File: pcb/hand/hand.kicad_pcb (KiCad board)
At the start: 2 copper layers, 174 x 125.2 mm, 47 parts, among them J1 Conn_01x15, J2 Conn_01x15

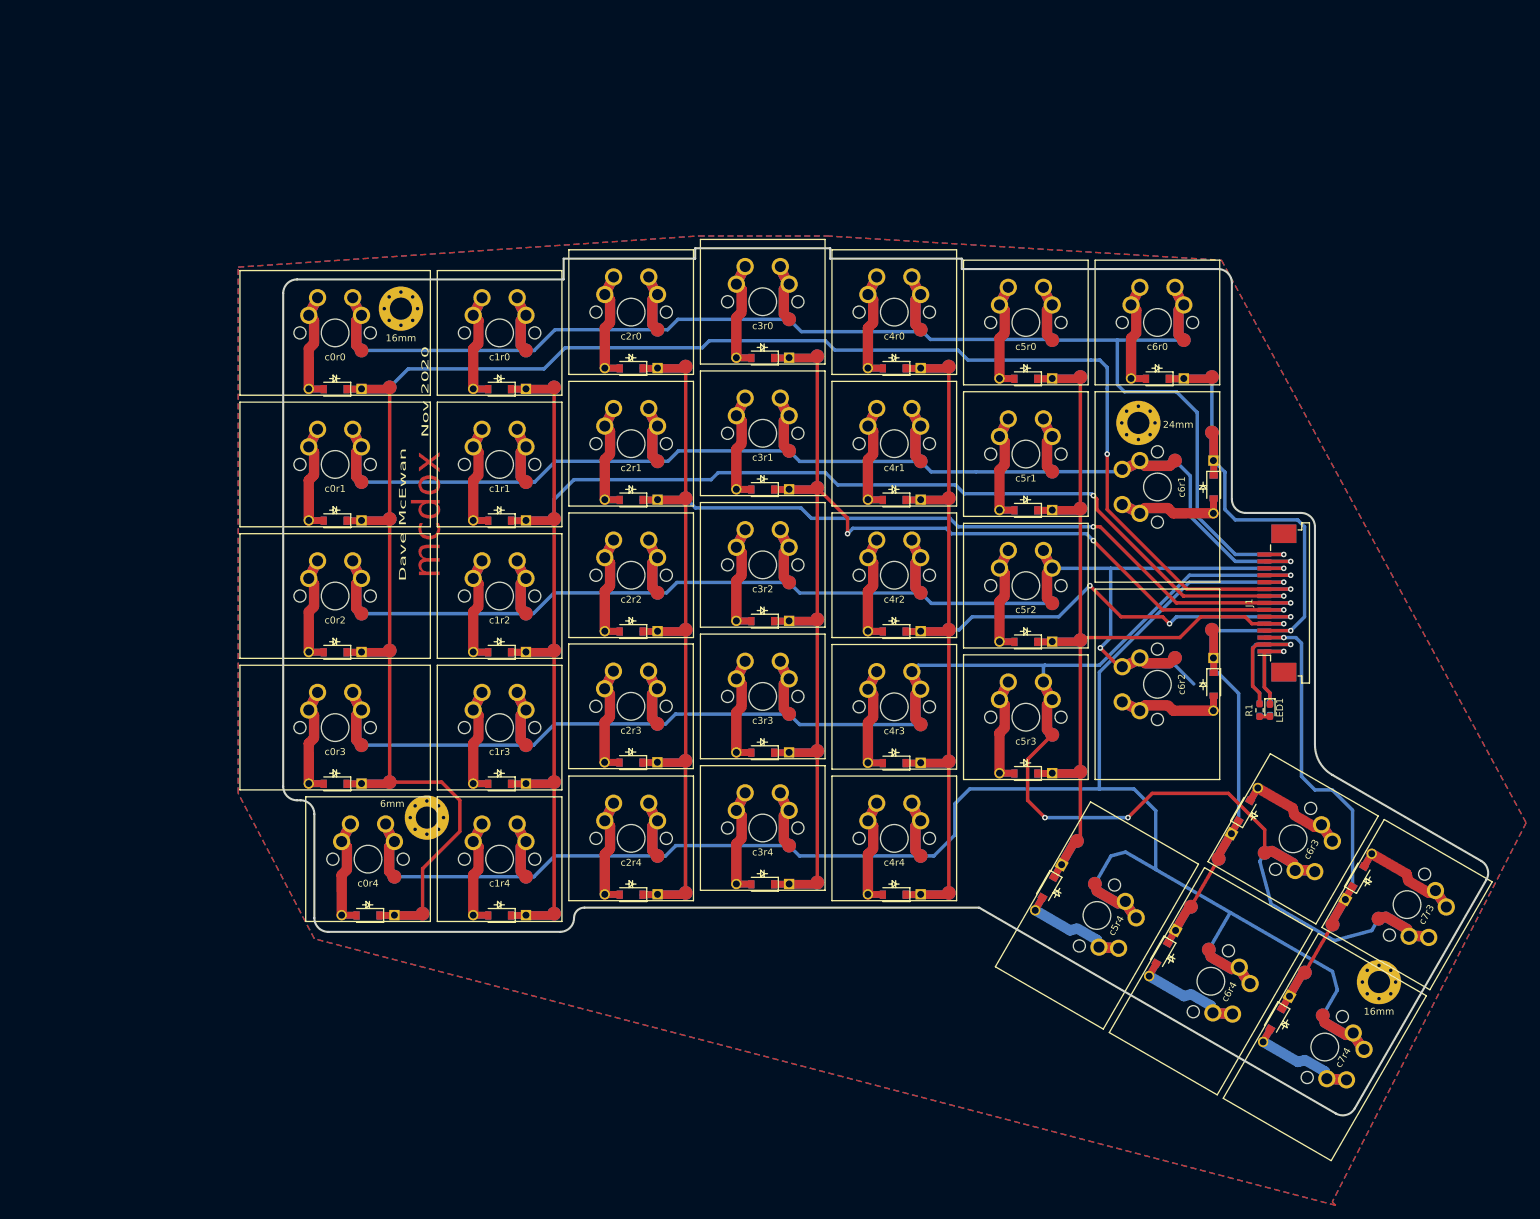
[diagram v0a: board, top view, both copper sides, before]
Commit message: pcb/hand Begin layout and edges.
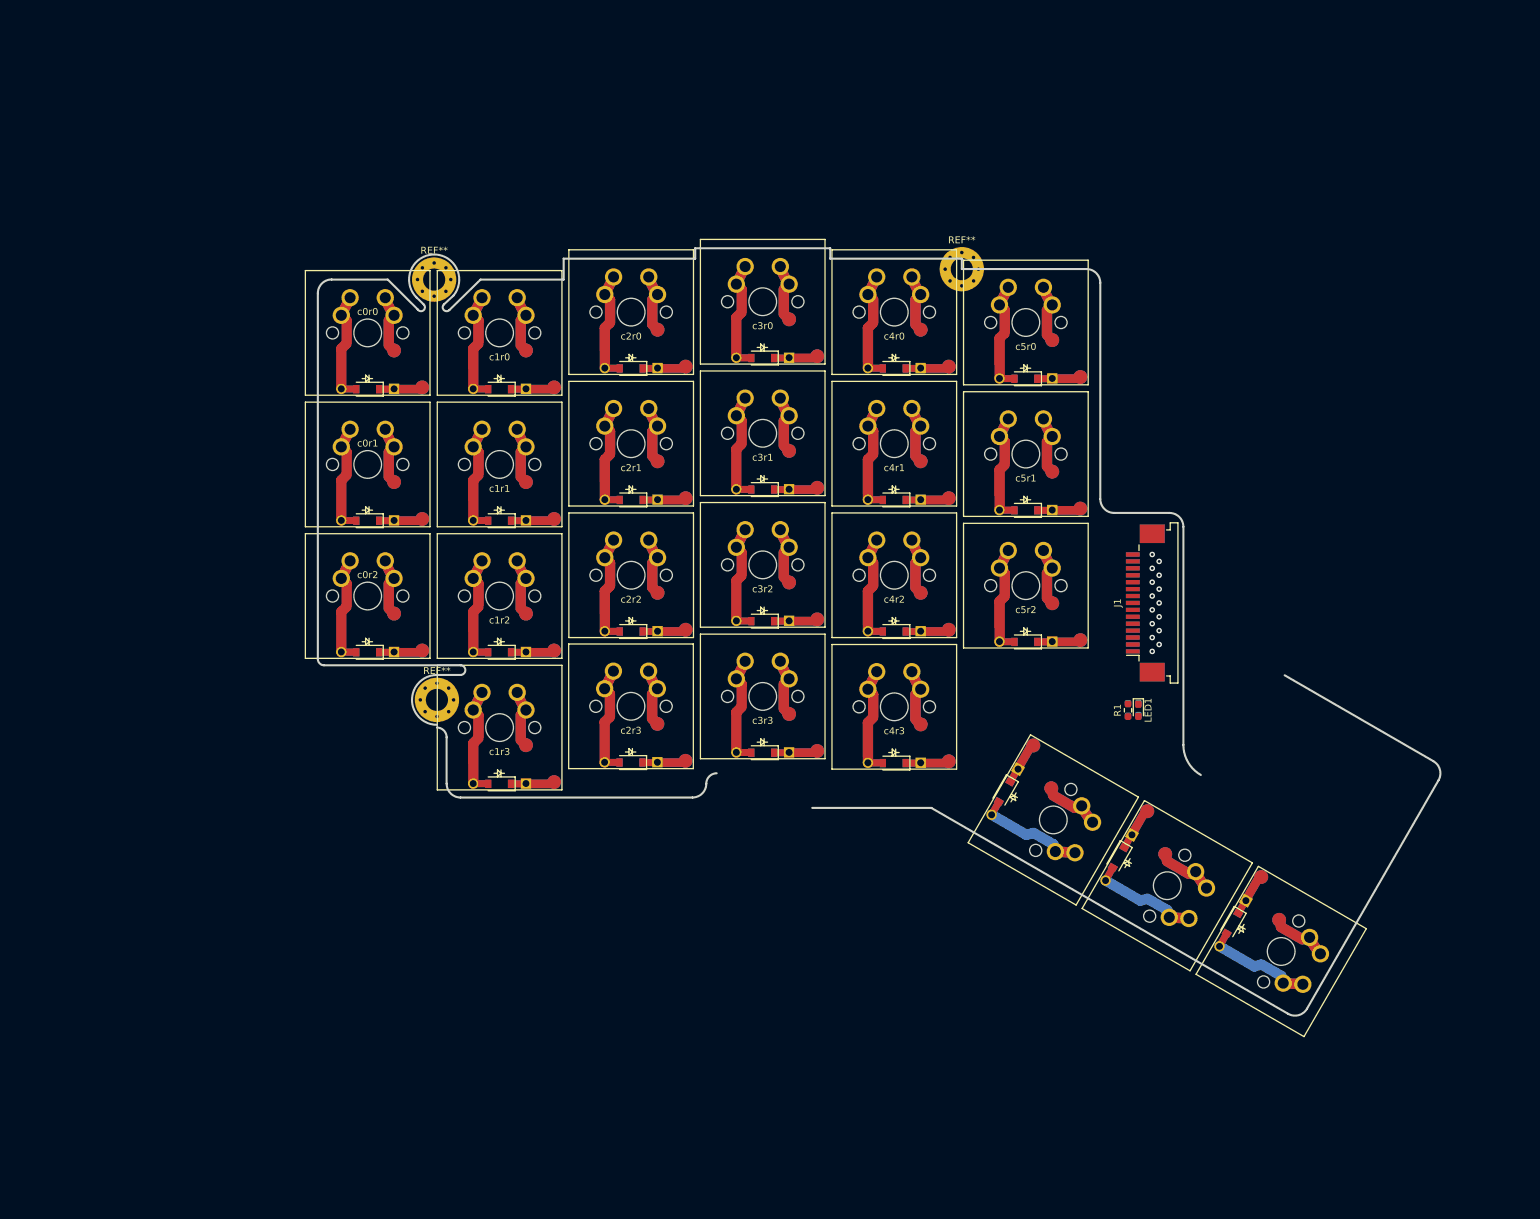
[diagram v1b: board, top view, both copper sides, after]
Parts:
- removed 16mm (x2), 24mm, 6mm: MountingHole_3.2mm_M3_Pad_Via, hand:MountingHole_3.2mm_M3_Pad_Via
- removed c0r3, c5r4, c6r4, c7r4: switchDiode, hand:reversibleMX_15u
- removed c0r4, c1r4, c2r4, c3r4, c4r4, c5r3, c6r0, c7r3: switchDiode, hand:reversibleMX_10u
- added REF**: MountingHole_3.2mm_M3_Pad_Via, hand:MountingHole_3.2mm_M3_Pad_Via, F.Cu at (58.7, 92.0)
- added REF**: MountingHole_3.2mm_M3_Pad_Via, hand:MountingHole_3.2mm_M3_Pad_Via, F.Cu at (134.5, 29.8)
- added REF**: MountingHole_3.2mm_M3_Pad_Via, hand:MountingHole_3.2mm_M3_Pad_Via, F.Cu at (58.3, 31.3)
- R1, R2: value 100 -> 220
- c0r0, c0r1, c0r2: footprint hand:reversibleMX_15u -> hand:reversibleMX_10u
- c6r1, c6r2: footprint hand:reversibleMX_15u -> hand:reversibleMX_10u; moved to B.Cu
- c6r3: moved to B.Cu
- moved c6r1 69.4 mm to (180.6, 128.3), turned to 60 degrees
- moved c6r3 34.7 mm to (147.7, 109.3), turned to 60 degrees
- moved c6r2 29.1 mm to (164.2, 118.8), turned to 60 degrees
- moved J1 19.0 mm to (161.0, 78.0)
- moved J2 19.0 mm to (161.0, 78.0)
- moved LED1 19.0 mm to (160.0, 93.5)
- moved LED2 19.0 mm to (160.0, 93.4)
- moved R1 19.0 mm to (158.5, 93.5)
- moved R2 19.0 mm to (158.5, 93.4)
- moved c0r0 4.70 mm to (48.7, 39.0)
- moved c0r1 4.70 mm to (48.7, 58.0)
- moved c0r2 4.70 mm to (48.7, 77.0)
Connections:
- J1 pad 11: row4 -> Net-(J1-Pad11)
- J1 pad 3: col7 -> Net-(J1-Pad3)
- J2 pad 13: col7 -> Net-(J2-Pad13)
- J2 pad 5: row4 -> Net-(J2-Pad5)
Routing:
- net col0: track 313.4 -> 0.00 mm, vias 2 -> 1
- net row4: track 271.5 -> 0.00 mm
- net row3: track 265.5 -> 0.00 mm, vias 3 -> 1
- net col1: track 261.9 -> 0.00 mm, vias 2 -> 1
- net col2: track 238.5 -> 0.00 mm, vias 2 -> 1
- net col3: track 220.5 -> 0.00 mm, vias 3 -> 1
- net row0: track 206.9 -> 0.00 mm
- net col4: track 199.6 -> 0.00 mm, vias 3 -> 1
- net row2: track 191.9 -> 0.00 mm, vias 2 -> 1
- net row1: track 174.9 -> 0.00 mm
- net col5: track 164.6 -> 0.00 mm
- net col6: track 152.3 -> 0.00 mm
- net col7: track 80.6 -> 0.00 mm
- net +3V3: track 28.3 -> 0.00 mm
- net GND: track 21.4 -> 0.00 mm
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- removed copper zone on B.Cu, net (none)
- removed copper zone on F.Cu, net (none)
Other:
- board size 174 x 125.2 mm -> 162.1 x 110.8 mm
- board text removed: "Dave McEwan"
- board text removed: "Nov 2020"
- board text removed: "c0r5"
- board text removed: "c0r6"
- board text removed: "c1r5"
- board text removed: "c2r5"
- board text removed: "c3r5"
- board text removed: "c4r5"
- board text removed: "c5r5"
- board text removed: "c5r6"
- board text removed: "c6r5"
- board text removed: "c6r6"
- board text removed: "c6r7"
- board text removed: "c6r8"
- board text removed: "c6r9"
- board text removed: "c7r5"
- board text removed: "c7r6"

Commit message: pcb/hand Layout finger cluster.
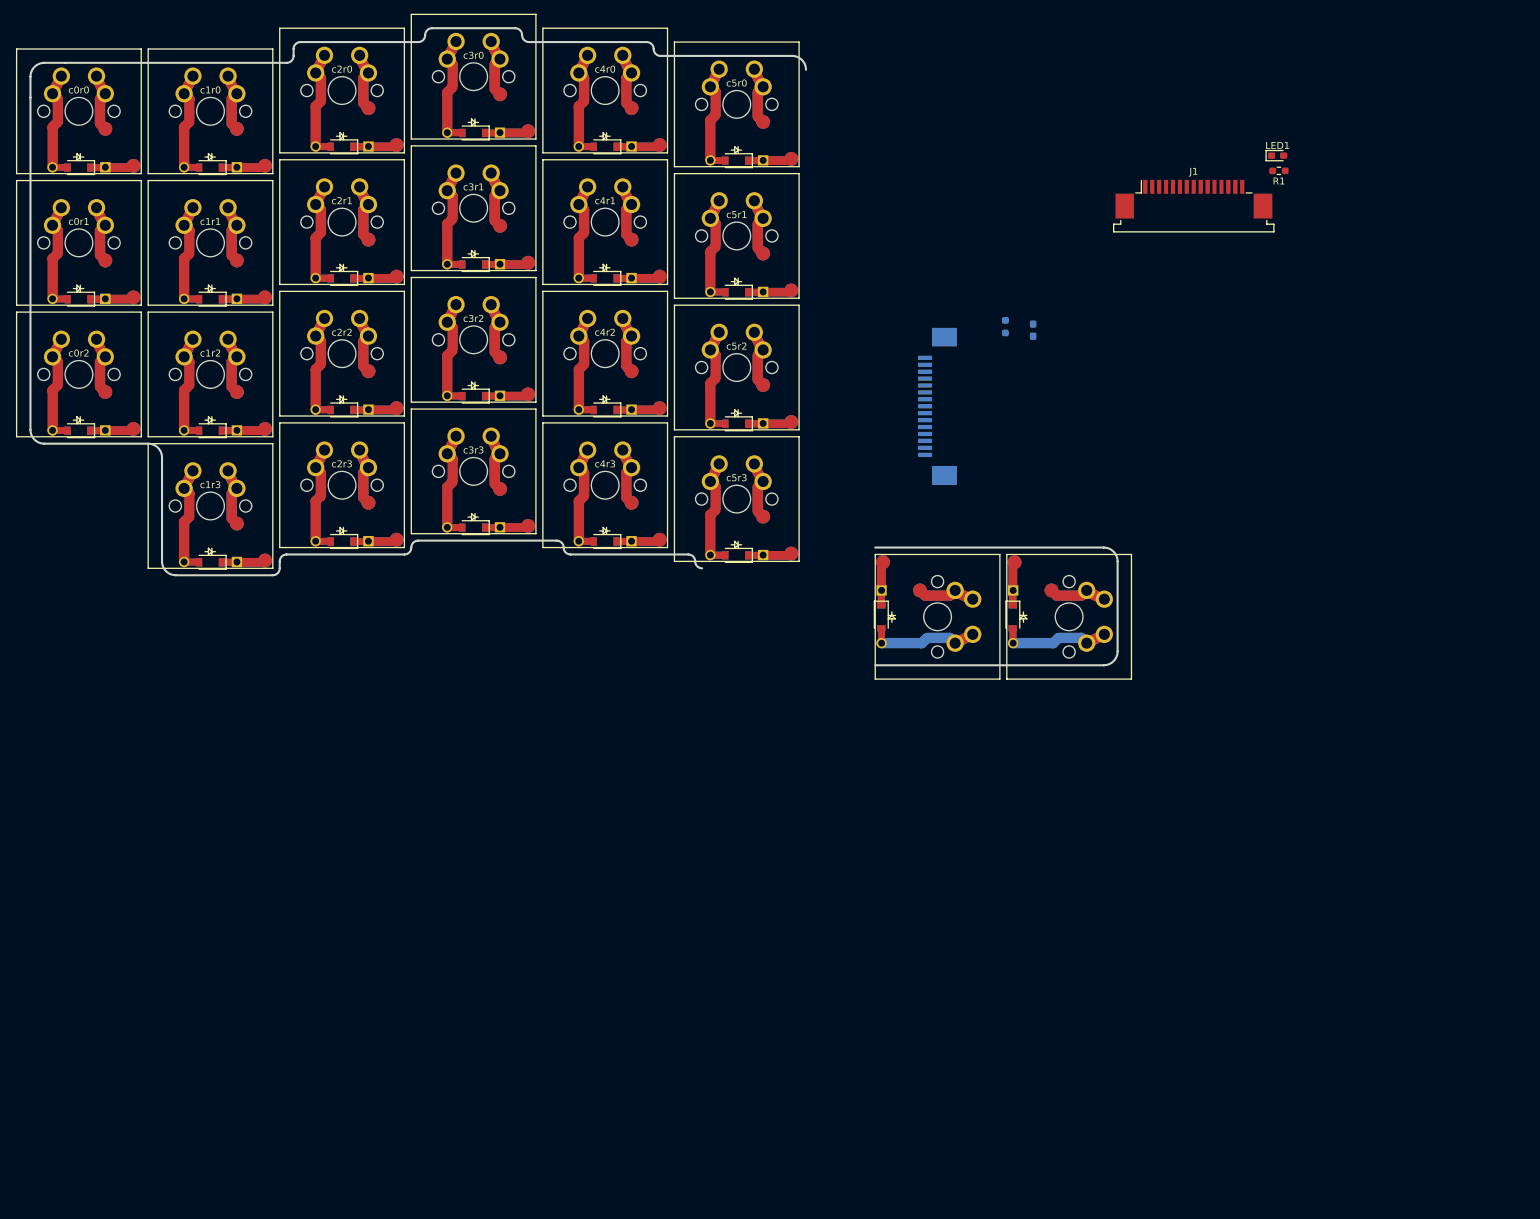
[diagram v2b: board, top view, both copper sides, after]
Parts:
- removed REF** (x3): MountingHole_3.2mm_M3_Pad_Via, hand:MountingHole_3.2mm_M3_Pad_Via
- removed c6r1: switchDiode, hand:reversibleMX_10u
- added c5r3: switchDiode, hand:reversibleMX_10u, F.Cu at (102.0, 63.0)
- moved LED1 82.6 mm to (180.1, 13.4), turned to 0 degrees
- moved R1 80.9 mm to (180.3, 15.6), turned to 0 degrees
- moved J1 58.7 mm to (168.0, 19.7), turned to 0 degrees
- moved R2 58.1 mm to (140.8, 38.1)
- moved LED2 56.8 mm to (144.8, 38.6)
- moved c3r0 52.9 mm to (64.0, 2.00)
- moved c3r1 52.9 mm to (64.0, 21.0)
- moved c3r2 52.9 mm to (64.0, 40.0)
- moved c3r3 52.9 mm to (64.0, 59.0)
- moved c1r0 52.6 mm to (26.0, 7.00)
- moved c1r1 52.6 mm to (26.0, 26.0)
- moved c1r2 52.6 mm to (26.0, 45.0)
- moved c1r3 52.6 mm to (26.0, 64.0)
- moved c2r0 52.6 mm to (45.0, 4.00)
- moved c2r1 52.6 mm to (45.0, 23.0)
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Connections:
- J1 pad 11: Net-(J1-Pad11) -> (no net)
- J1 pad 3: Net-(J1-Pad3) -> (no net)
- J2 pad 13: Net-(J2-Pad13) -> (no net)
- J2 pad 5: Net-(J2-Pad5) -> (no net)
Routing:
- net row4: vias 1 -> 0
- net row3: vias 1 -> 0
- net row2: vias 1 -> 0
- net row1: vias 1 -> 0
- net row0: vias 1 -> 0
- net col7: vias 1 -> 0
- net col6: vias 1 -> 0
- net col5: vias 1 -> 0
- net col4: vias 1 -> 0
- net col3: vias 1 -> 0
- net col2: vias 1 -> 0
- net col1: vias 1 -> 0
- net col0: vias 1 -> 0
- net GND: vias 1 -> 0
- net +3V3: vias 1 -> 0
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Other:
- board size 162.1 x 110.8 mm -> 157 x 92 mm
- board text removed: "c0r7"
- board text removed: "c0r8"
- board text removed: "c0r9"
- board text removed: "c1r6"
- board text removed: "c1r7"
- board text removed: "c1r8"
- board text removed: "c1r9"
- board text removed: "c2r6"
- board text removed: "c2r7"
- board text removed: "c2r8"
- board text removed: "c2r9"
- board text removed: "c3r6"
- board text removed: "c3r7"
- board text removed: "c3r8"
- board text removed: "c3r9"
- board text removed: "c4r6"
- board text removed: "c4r7"
- board text removed: "c4r8"
- board text removed: "c4r9"
- board text removed: "c5r7"
- board text removed: "c5r8"
- board text removed: "c5r9"

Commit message: pcb/hand Route and fill
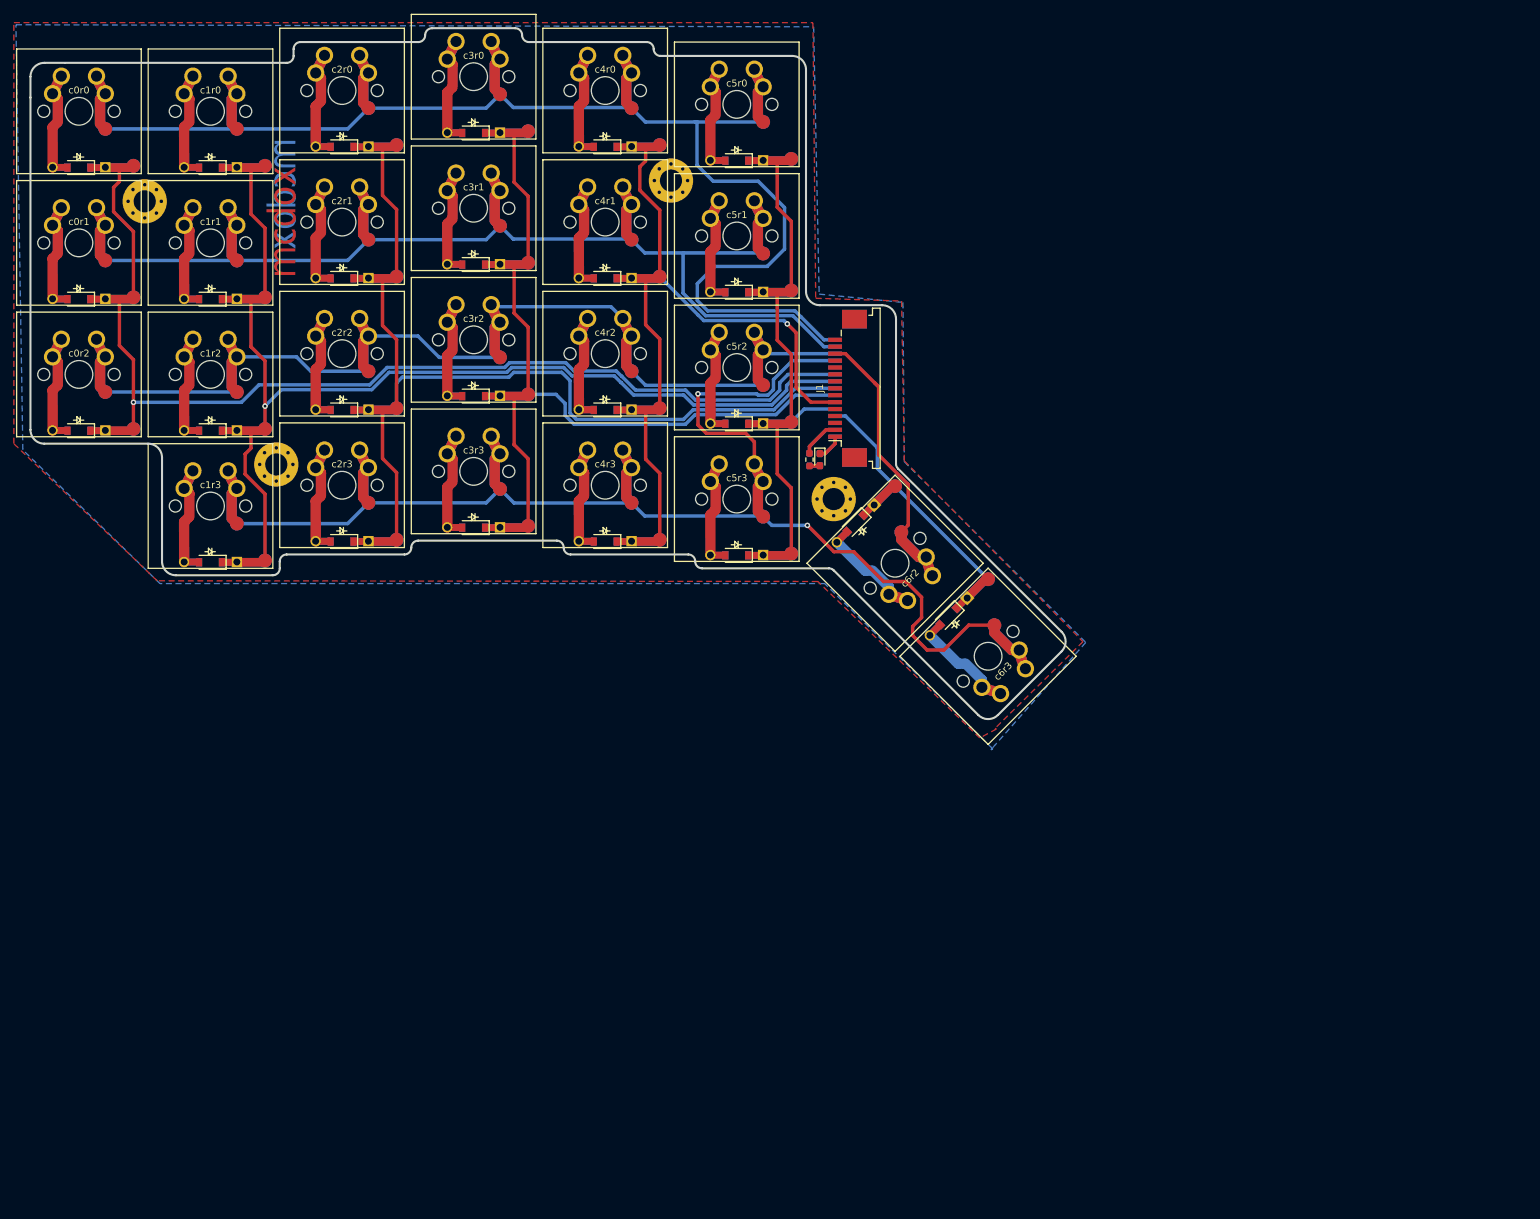
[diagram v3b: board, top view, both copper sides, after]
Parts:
- added REF**: MountingHole_3.2mm_M3_Pad_Via, MountingHole:MountingHole_3.2mm_M3_Pad_Via, F.Cu at (116.0, 63.0)
- added REF**: MountingHole_3.2mm_M3_Pad_Via, MountingHole:MountingHole_3.2mm_M3_Pad_Via, F.Cu at (92.5, 17.0)
- added REF**: MountingHole_3.2mm_M3_Pad_Via, MountingHole:MountingHole_3.2mm_M3_Pad_Via, F.Cu at (16.5, 20.0)
- added REF**: MountingHole_3.2mm_M3_Pad_Via, MountingHole:MountingHole_3.2mm_M3_Pad_Via, F.Cu at (35.5, 58.0)
- moved R1 79.6 mm to (112.5, 57.3), turned to 270 degrees
- moved LED1 79.3 mm to (114.0, 57.3), turned to 270 degrees
- moved J1 57.0 mm to (118.0, 47.0), turned to 90 degrees
- moved LED2 36.0 mm to (114.0, 57.3)
- moved R2 34.2 mm to (112.5, 57.3)
- moved J2 13.3 mm to (118.0, 47.0)
- moved c6r3 13.0 mm to (138.3, 85.7), turned to 45 degrees
- moved c6r2 9.87 mm to (124.9, 72.3), turned to 45 degrees
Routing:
- net row3: track 0.00 -> 185.7 mm, vias 0 -> 2
- net row0: track 0.00 -> 184.5 mm
- net col1: track 0.00 -> 173.0 mm, vias 0 -> 1
- net col0: track 0.00 -> 167.1 mm, vias 0 -> 1
- net row2: track 0.00 -> 162.9 mm
- net col2: track 0.00 -> 159.3 mm
- net row1: track 0.00 -> 148.1 mm
- net col3: track 0.00 -> 133.1 mm
- net col4: track 0.00 -> 121.8 mm, vias 0 -> 1
- net col5: track 0.00 -> 91.3 mm
- net col6: track 0.00 -> 45.1 mm
- net +3V3: track 0.00 -> 11.4 mm
- net GND: track 0.00 -> 7.58 mm
- net Net-(LED2-Pad2): track 0.00 -> 1.52 mm
- net Net-(LED1-Pad2): track 0.00 -> 1.52 mm
- added copper zone on B.Cu, net (none)
- added copper zone on F.Cu, net (none)
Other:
- board size 157 x 92 mm -> 149.5 x 99.8 mm
- board text added: "c0r5"
- board text added: "c0r6"
- board text added: "c0r7"
- board text added: "c1r4"
- board text added: "c1r5"
- board text added: "c1r6"
- board text added: "c1r7"
- board text added: "c2r4"
- board text added: "c2r5"
- board text added: "c2r6"
- board text added: "c2r7"
- board text added: "c3r4"
- board text added: "c3r5"
- board text added: "c3r6"
- board text added: "c3r7"
- board text added: "c4r4"
- board text added: "c4r5"
- board text added: "c4r6"
- board text added: "c4r7"
- board text added: "c5r4"
- board text added: "c5r5"
- board text added: "c5r6"
- board text added: "c5r7"
- board text added: "c6r4"
- board text added: "c6r5"
